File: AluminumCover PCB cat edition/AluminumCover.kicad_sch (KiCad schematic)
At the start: 8 parts, among them P2 RoundConnectorPad, P3 RoundConnectorPad, P4 RoundConnectorPad, P5 RoundConnectorPad, P6 RoundConnectorPad, P7 RoundConnectorPad, P8 RoundConnectorPad

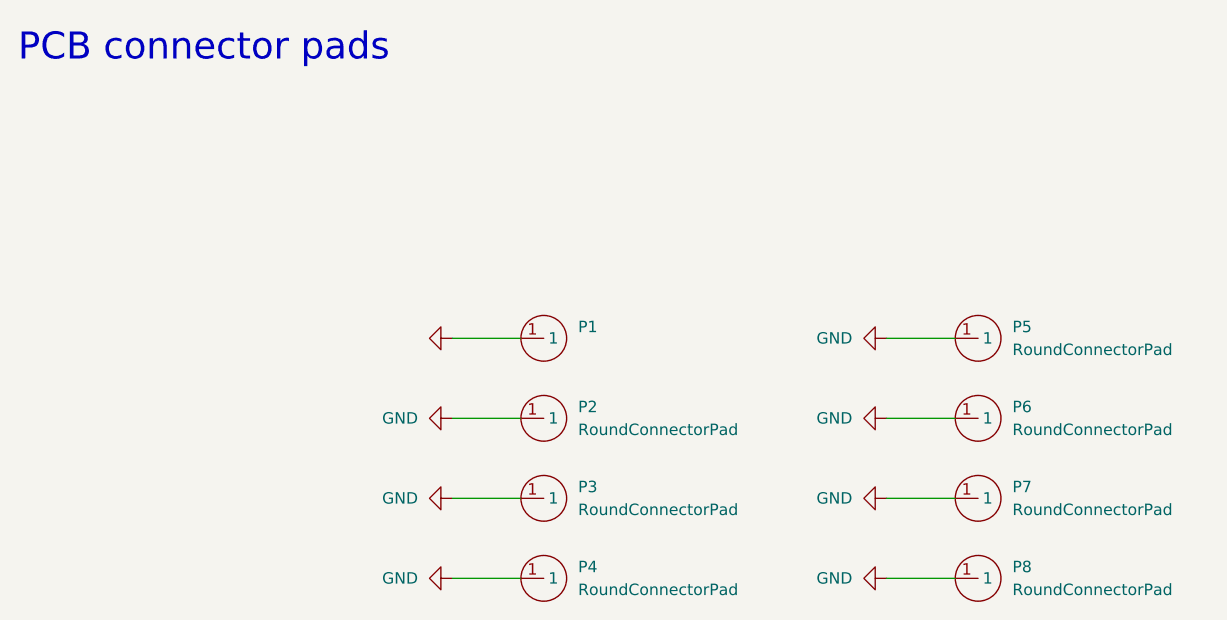
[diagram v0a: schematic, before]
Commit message: made improvements and started creating usb-c only version
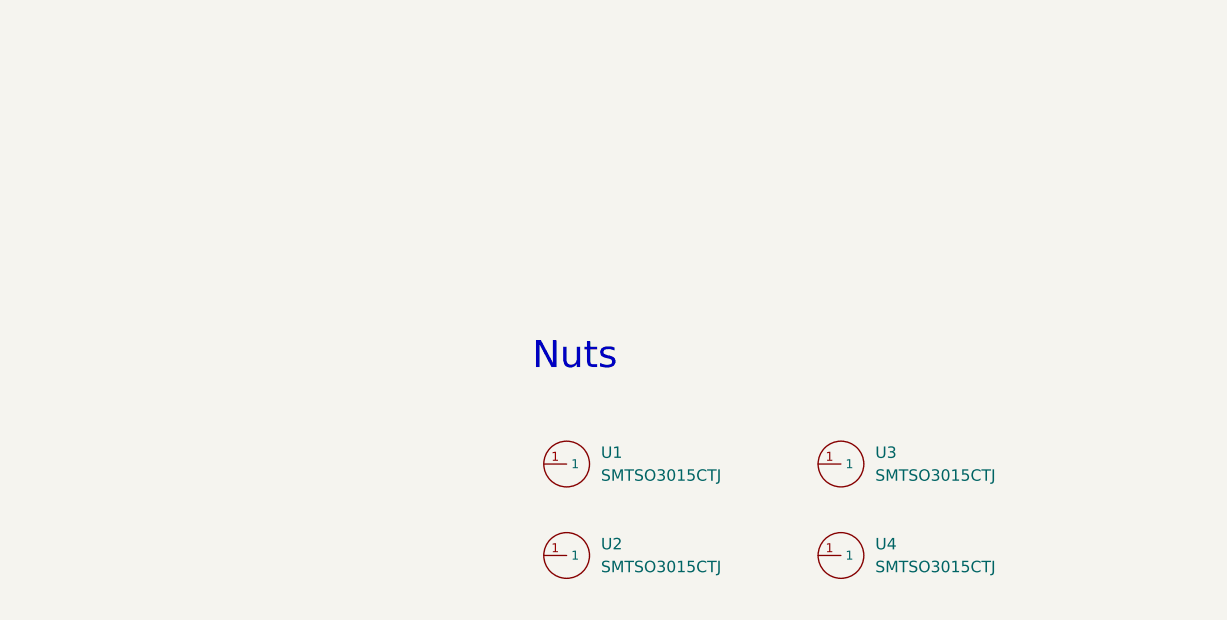
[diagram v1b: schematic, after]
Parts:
- removed P1: (no value), symbol MyParts:RoundConnectorPad
- removed P2, P3, P4, P5, P6, P7, P8: RoundConnectorPad, footprint:RoundSolderPad, symbol MyParts:RoundConnectorPad
- added U1, U2, U3, U4: SMTSO3015CTJ, footprint:SMTSO3030CTJ, symbol MyParts:SMTSO3015CTJ
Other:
- note added: "Nuts"
- note removed: "PCB connector pads"
